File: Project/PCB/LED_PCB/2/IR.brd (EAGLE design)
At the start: 60 x 60 mm, 27 parts

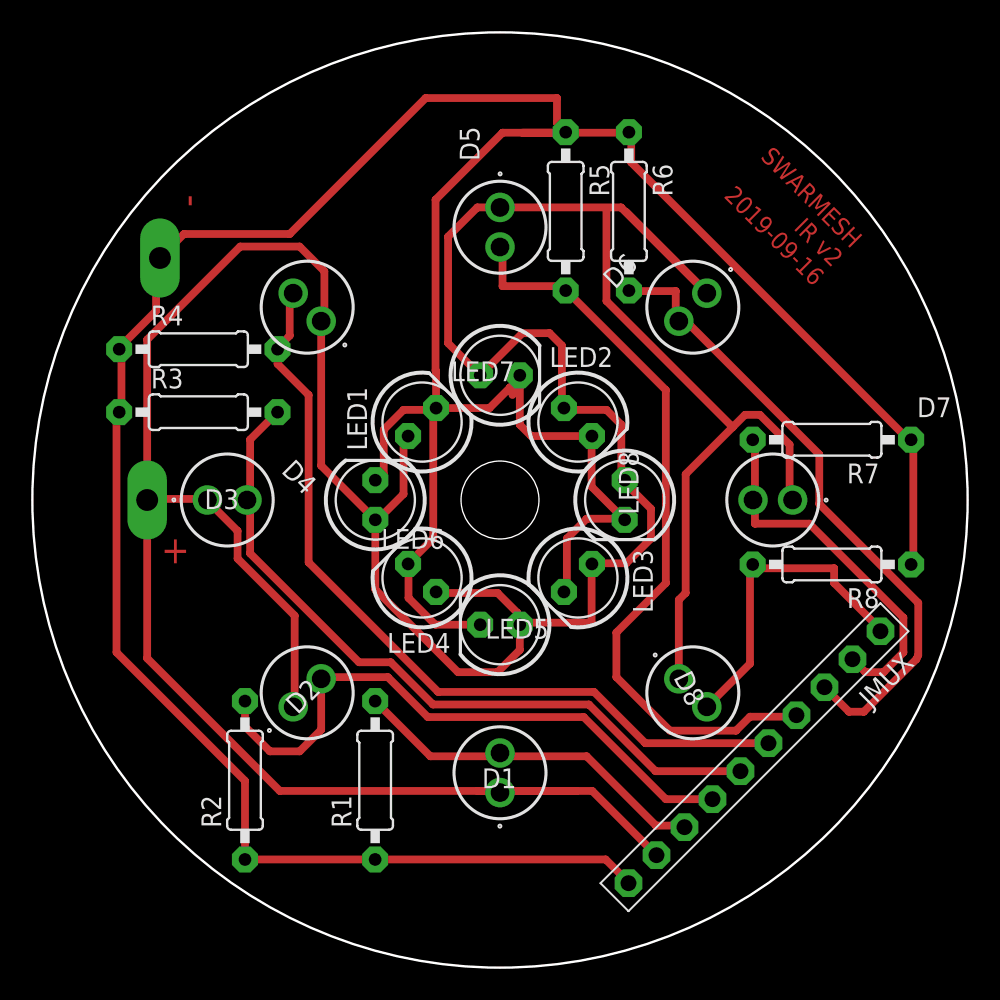
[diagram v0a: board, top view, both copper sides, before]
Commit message: modified tracks IR pcb
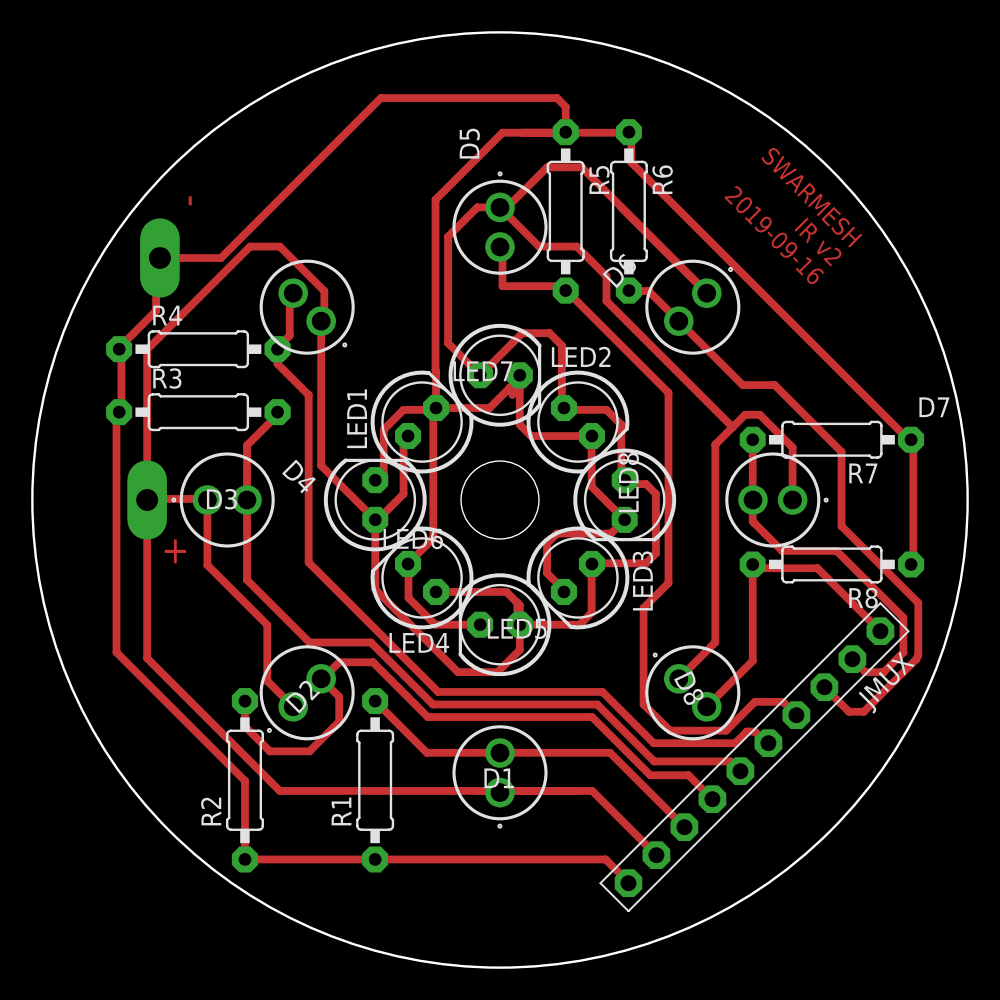
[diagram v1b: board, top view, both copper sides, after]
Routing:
- net VCC: track 264.7 -> 273.7 mm
- net N$2: track 39.4 -> 41.5 mm
- net GND: track 222.6 -> 223.9 mm
- net N$6: track 42.6 -> 41.2 mm
- net N$3: track 47.2 -> 48.6 mm
- net N$4: track 52.8 -> 53.4 mm
- net N$5: track 48.9 -> 48.3 mm
- net N$8: track 20.9 -> 20.4 mm

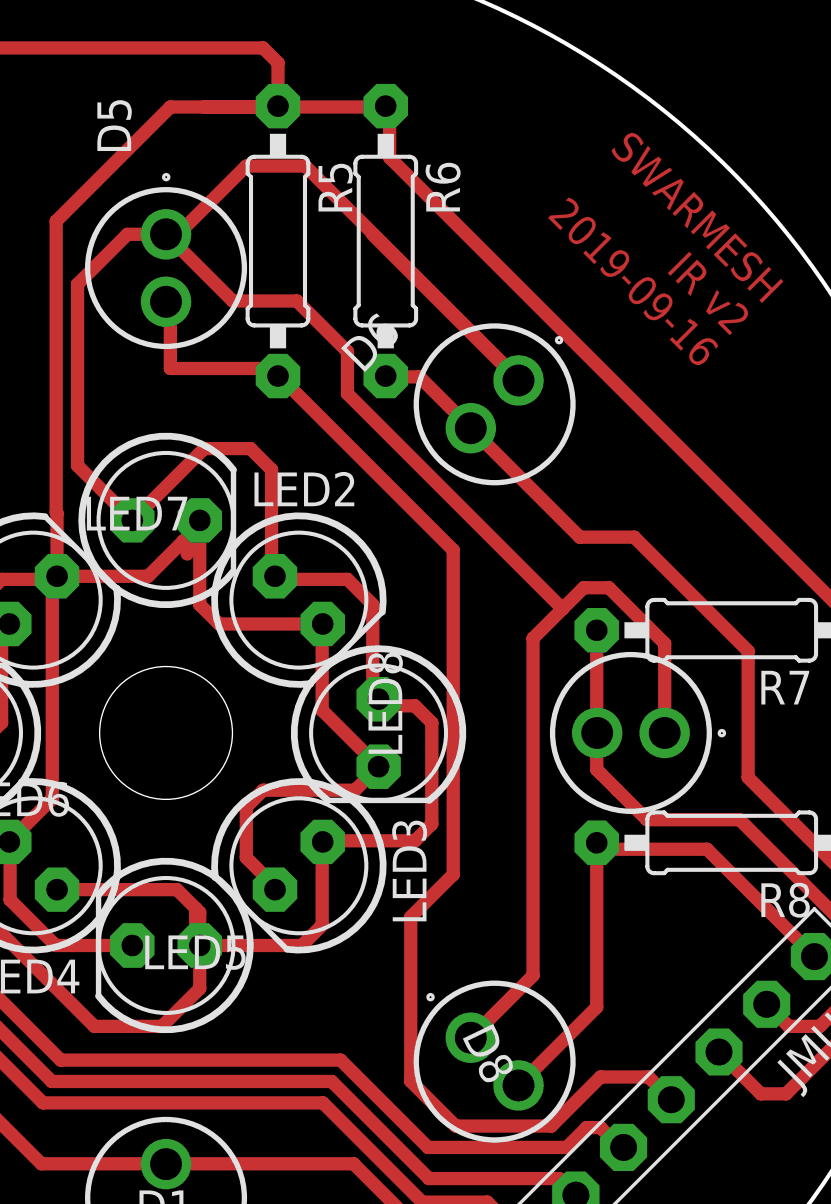
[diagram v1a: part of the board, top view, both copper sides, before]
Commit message: modified tracks IR pcb2
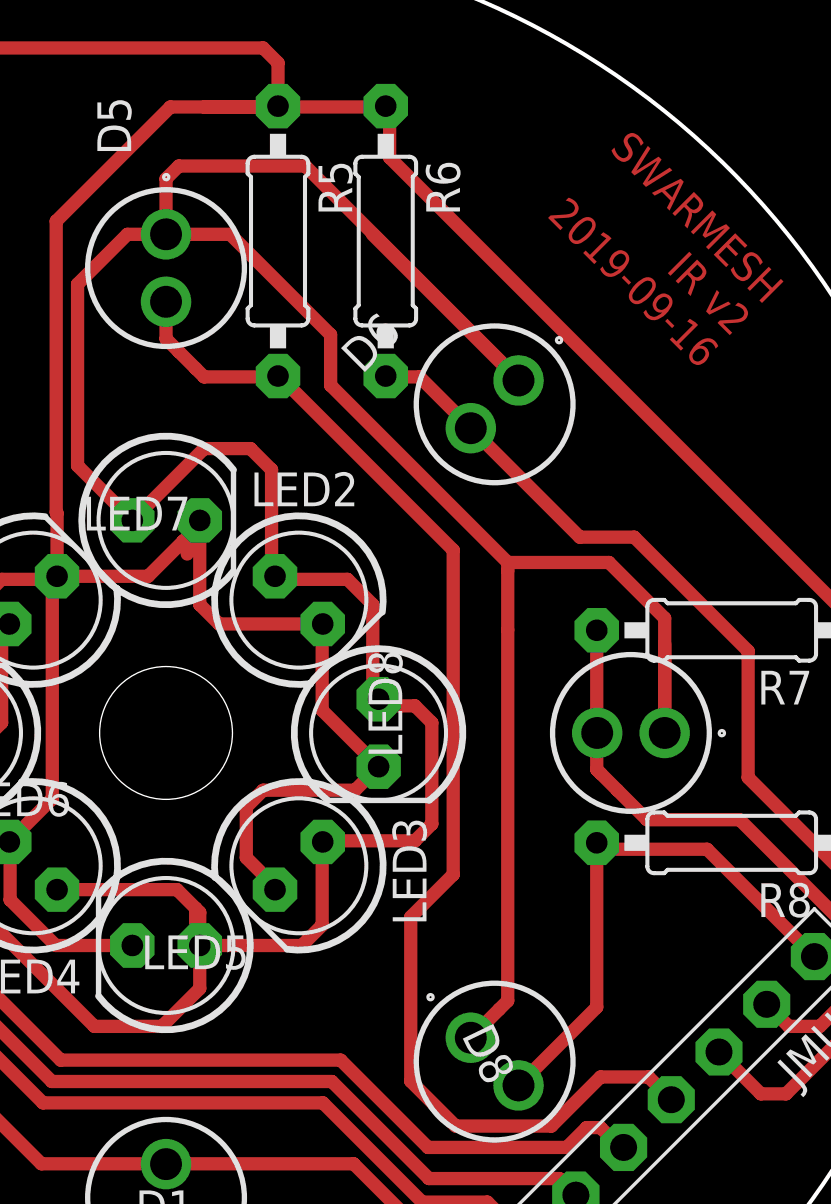
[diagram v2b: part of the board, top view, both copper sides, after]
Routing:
- net VCC: track 273.7 -> 279.3 mm
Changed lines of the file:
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@@
 <contactref element="R5" pad="2"/>
 <contactref element="JMUX" pad="4"/>
-<wire x1="30.1625" y1="45.72" x2="33.9725" y2="45.72" width="0.5" layer="1"/>
-<wire x1="30.1625" y1="47.9425" x2="30.1625" y2="45.72" width="0.5" layer="1"/>
-<wire x1="33.9725" y1="45.72" x2="34.215" y2="45.4348" width="0.5" layer="1"/>
-<wire x1="30" y1="48.23" x2="30.1625" y2="47.9425" width="0.5" layer="1"/>
 <wire x1="34.215" y1="45.4348" x2="34.29" y2="45.4025" width="0.5" layer="1"/>
 <wire x1="39.21125" y1="18.89125" x2="40.899675" y2="17.202825" width="0.5" layer="1"/>
@@
 <wire x1="40.8098" y1="26.67" x2="39.21125" y2="25.07145" width="0.5" layer="1"/>
 <wire x1="39.21125" y1="25.07145" x2="39.21125" y2="18.89125" width="0.5" layer="1"/>
+<wire x1="30" y1="48.23" x2="30" y2="46.835" width="0.5" layer="1"/>
+<wire x1="30" y1="46.835" x2="30.48" y2="46.355" width="0.5" layer="1"/>
+<wire x1="30.48" y1="46.355" x2="31.115" y2="45.72" width="0.5" layer="1"/>
+<wire x1="31.115" y1="45.72" x2="31.4325" y2="45.4025" width="0.5" layer="1"/>
+<wire x1="31.4325" y1="45.4025" x2="34.29" y2="45.4025" width="0.5" layer="1"/>
 </signal>
 <signal name="N$6">
@@
 <wire x1="46.99" y1="29.845" x2="48.10125" y2="28.73375" width="0.5" layer="1"/>
 <wire x1="48.10125" y1="28.73375" x2="51.59375" y2="28.73375" width="0.5" layer="1"/>
-<wire x1="46.355" y1="30.48" x2="46.213015625" y2="30.621984375" width="0.5" layer="1"/>
-<wire x1="46.213015625" y1="30.621984375" x2="46.213015625" y2="35.865" width="0.5" layer="1"/>
+<wire x1="46.213015625" y1="30.621984375" x2="46.355" y2="30.48" width="0.5" layer="1"/>
+<wire x1="46.213015625" y1="35.865" x2="46.213015625" y2="30.621984375" width="0.5" layer="1"/>
 <wire x1="46.213015625" y1="30.621984375" x2="46.355" y2="31.875" width="0" layer="19" extent="1-1"/>
 </signal>
@@
 <contactref element="LED1" pad="A"/>
 <contactref element="JMUX" pad="9"/>
-<wire x1="45.72" y1="37.465" x2="44.92625" y2="36.67125" width="0.5" layer="1"/>
-<wire x1="46.6725" y1="37.465" x2="45.72" y2="37.465" width="0.5" layer="1"/>
 <wire x1="35.898025" y1="27.898025" x2="36.195" y2="27.94" width="0.5" layer="1"/>
 <wire x1="34.101971875" y1="37.898025" x2="34.29" y2="37.7825" width="0.5" layer="1"/>
@@
 <wire x1="35.8775" y1="24.765" x2="35.8775" y2="27.6225" width="0.5" layer="1"/>
 <wire x1="35.8775" y1="27.6225" x2="35.898025" y2="27.898025" width="0.5" layer="1"/>
-<wire x1="36.83" y1="44.7675" x2="44.92625" y2="36.67125" width="0.5" layer="1"/>
 <wire x1="40.005" y1="9.525" x2="40.03881875" y2="9.21381875" width="0.5" layer="1"/>
 <wire x1="11.1125" y1="32.0675" x2="7.62" y2="32.0675" width="0.5" layer="1"/>
@@
 <wire x1="28.73" y1="40" x2="31.43375" y2="42.70375" width="0.5" layer="1"/>
 <wire x1="31.43375" y1="42.70375" x2="33.17875" y2="42.70375" width="0.5" layer="1"/>
-<wire x1="43.815" y1="35.56" x2="44.92625" y2="36.67125" width="0.5" layer="1"/>
 <wire x1="28.73" y1="40" x2="26.67" y2="42.06" width="0.5" layer="1"/>
 <wire x1="26.67" y1="42.06" x2="26.67" y2="48.895" width="0.5" layer="1"/>
@@
 <wire x1="28.545" y1="50.77" x2="30" y2="50.77" width="0.5" layer="1"/>
 <wire x1="37.76605" y1="50.77" x2="43.268025" y2="45.268025" width="0.5" layer="1"/>
-<wire x1="35.2425" y1="53.34" x2="33.02" y2="53.34" width="0.5" layer="1"/>
-<wire x1="33.02" y1="53.34" x2="30.45" y2="50.77" width="0.5" layer="1"/>
-<wire x1="30.45" y1="50.77" x2="30" y2="50.77" width="0.5" layer="1"/>
-<wire x1="30" y1="50.77" x2="32.51" y2="48.26" width="0.5" layer="1"/>
-<wire x1="32.51" y1="48.26" x2="34.925" y2="48.26" width="0.5" layer="1"/>
-<wire x1="34.925" y1="48.26" x2="36.83" y2="46.355" width="0.5" layer="1"/>
-<wire x1="36.83" y1="46.355" x2="36.83" y2="44.7675" width="0.5" layer="1"/>
 <wire x1="38" y1="33.27" x2="38.25" y2="33.02" width="0.5" layer="1"/>
 <wire x1="39.37" y1="33.02" x2="38.25" y2="33.02" width="0.5" layer="1"/>
@@
 <wire x1="35.1125" y1="24" x2="31.27" y2="24" width="0.5" layer="1"/>
 <wire x1="11.23" y1="27.8225" x2="11.23" y2="32" width="0.5" layer="1"/>
-<wire x1="41.471971875" y1="20.528025" x2="43.815" y2="22.871053125" width="0.5" layer="1"/>
-<wire x1="43.815" y1="22.871053125" x2="43.815" y2="35.56" width="0.5" layer="1"/>
+<wire x1="41.471971875" y1="20.528025" x2="42.539471875" y2="21.595525" width="0.5" layer="1"/>
 <wire x1="48.77" y1="32" x2="48.77" y2="35.3675" width="0.5" layer="1"/>
-<wire x1="48.77" y1="35.3675" x2="46.6725" y2="37.465" width="0.5" layer="1"/>
 <wire x1="15.0702" y1="23.9823" x2="11.23" y2="27.8225" width="0.5" layer="1"/>
 <wire x1="16.731971875" y1="18.731971875" x2="15.0702" y2="20.39374375" width="0.5" layer="1"/>
@@
 <wire x1="7.365" y1="41.655" x2="7.365" y2="32" width="0.5" layer="1"/>
 <wire x1="18.7325" y1="43.18" x2="18.7325" y2="45.4025" width="0.5" layer="1"/>
+<wire x1="30" y1="50.77" x2="32.415" y2="50.77" width="0.5" layer="1"/>
+<wire x1="30" y1="50.77" x2="30" y2="52.86" width="0.5" layer="1"/>
+<wire x1="30" y1="52.86" x2="30.48" y2="53.34" width="0.5" layer="1"/>
+<wire x1="30.48" y1="53.34" x2="35.2425" y2="53.34" width="0.5" layer="1"/>
+<wire x1="36.195" y1="46.99" x2="36.195" y2="45.085" width="0.5" layer="1"/>
+<wire x1="36.195" y1="45.085" x2="42.8625" y2="38.4175" width="0.5" layer="1"/>
+<wire x1="32.415" y1="50.77" x2="36.195" y2="46.99" width="0.5" layer="1"/>
+<wire x1="46.6725" y1="38.4175" x2="48.77" y2="36.32" width="0.5" layer="1"/>
+<wire x1="48.77" y1="36.32" x2="48.77" y2="32" width="0.5" layer="1"/>
+<wire x1="42.8625" y1="38.4175" x2="46.6725" y2="38.4175" width="0.5" layer="1"/>
+<wire x1="42.8625" y1="35.8775" x2="42.8625" y2="38.1" width="0.5" layer="1"/>
+<wire x1="42.8625" y1="38.1" x2="42.8625" y2="38.4175" width="0.5" layer="1"/>
+<wire x1="42.8625" y1="35.8775" x2="42.8625" y2="21.918553125" width="0.5" layer="1"/>
+<wire x1="42.8625" y1="21.918553125" x2="42.539471875" y2="21.595525" width="0.5" layer="1"/>
 <wire x1="34.925" y1="13.335" x2="35.9176375" y2="13.335" width="0" layer="19" extent="1-1"/>
 </signal>
